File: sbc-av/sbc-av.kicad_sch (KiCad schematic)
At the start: 42 parts, among them J1 AVD-Header, J2 AVA-Header, Q1 PZT2222A, U1 MAX1683, U2 CD74HCT367E, U3 FMS6400

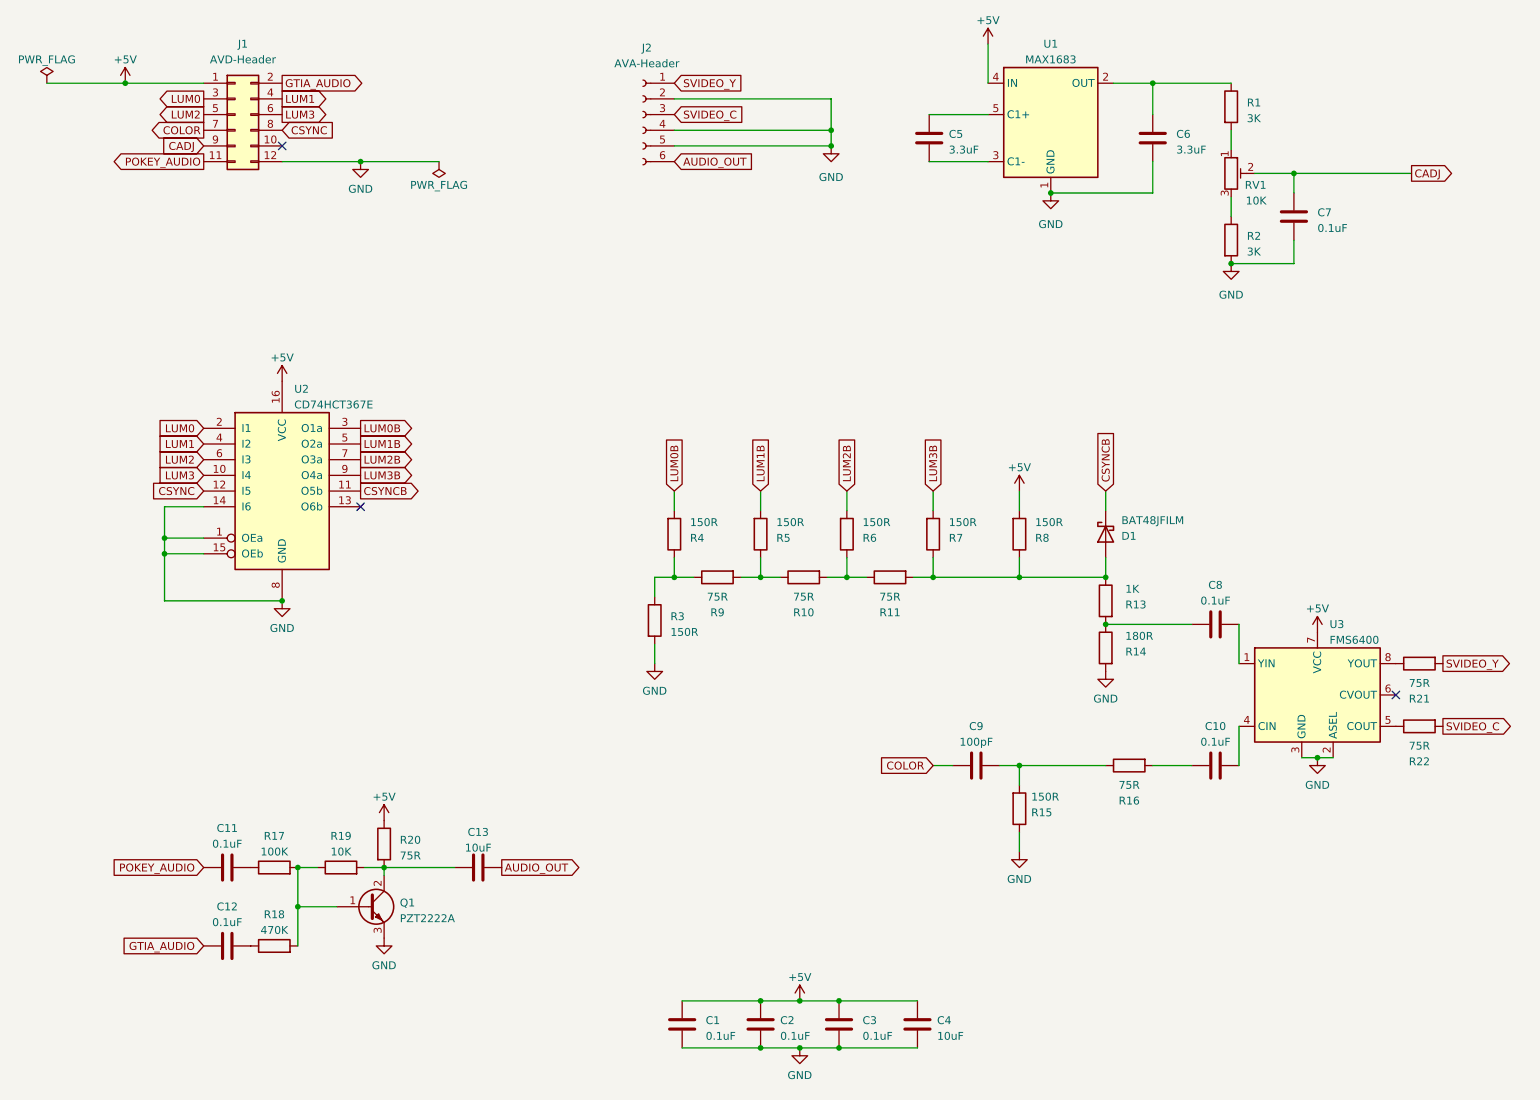
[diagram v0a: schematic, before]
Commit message: SBC v1.3
Motherboard updates:

  - KiCad 9 upgrade
  - USB-C power connector
  - Replace EOL resistor packs with discrete SMD resistors
  - Power/enable voltage translators from switched 5V
  - Fix motor signal pullup
  - Eliminate loop in phi2 traces
  - Thicker clock signal traces

SD card adapter updates:

  - KiCad 9 upgrade
  - Power/enable voltage translator from switched 5V and the eliminate unnecessary SIO pullups

Audio/Video adapter updates:

  - KiCad 9 upgrade
  - No functional changes, gerbers not regenerated, cleaned up bom
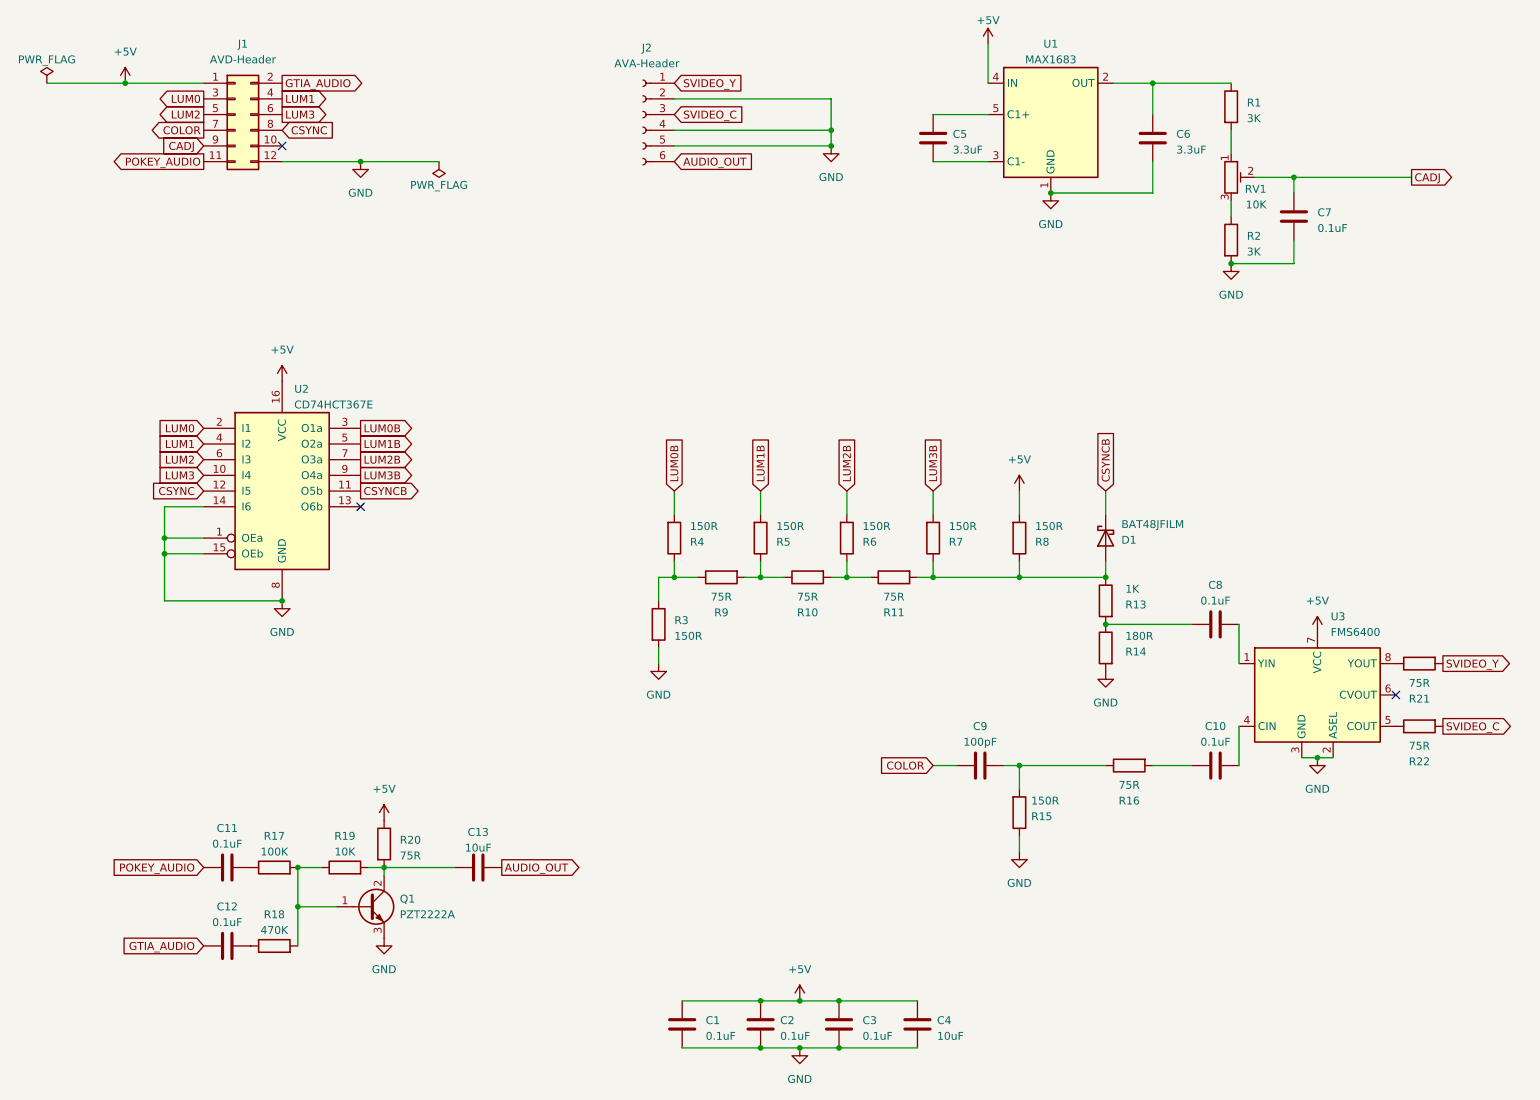
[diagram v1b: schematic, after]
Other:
- moved on the sheet: C5, C9, D1, R10, R11, R15, R19, R3, R4, R5, R6, R7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
